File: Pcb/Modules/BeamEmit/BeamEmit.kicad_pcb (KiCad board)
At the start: 2 copper layers, 50.8 x 20.3 mm, 10 parts, among them J1 JACK_RJ45, Q1 Q_NMOS_GSD, U3 TSOP585xx

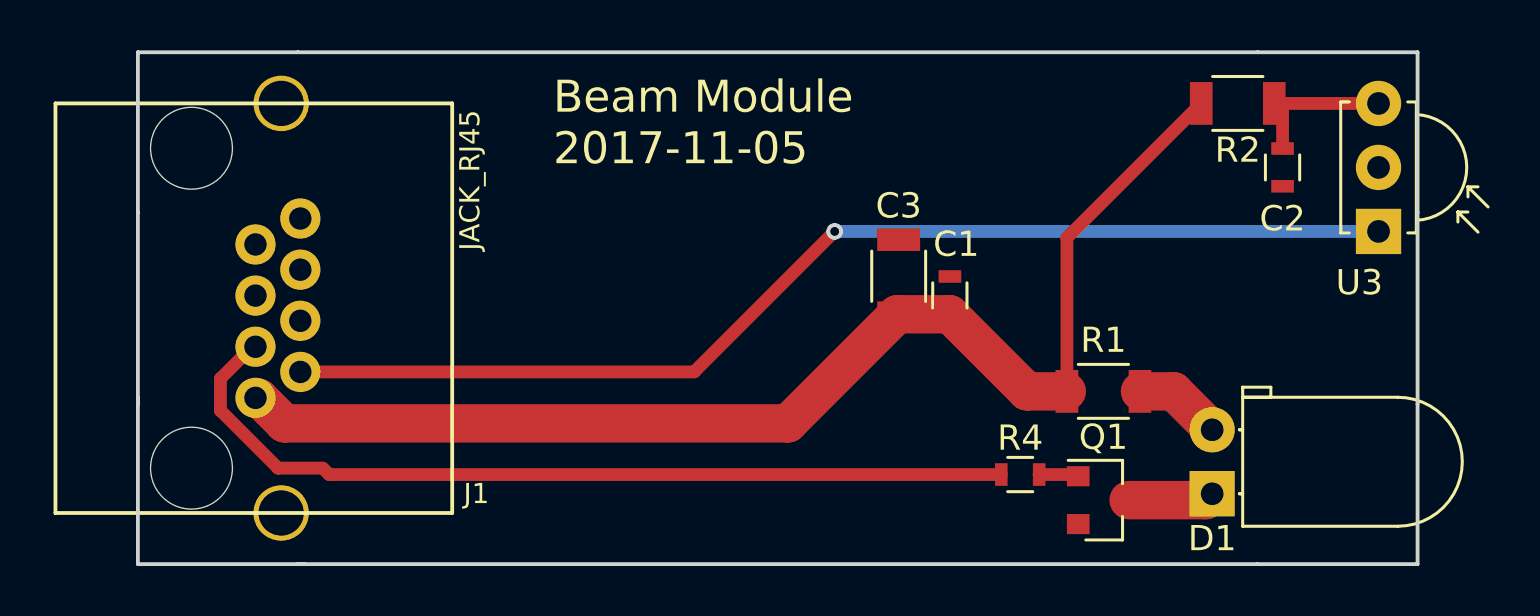
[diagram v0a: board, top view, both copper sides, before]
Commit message: Update module pcbs
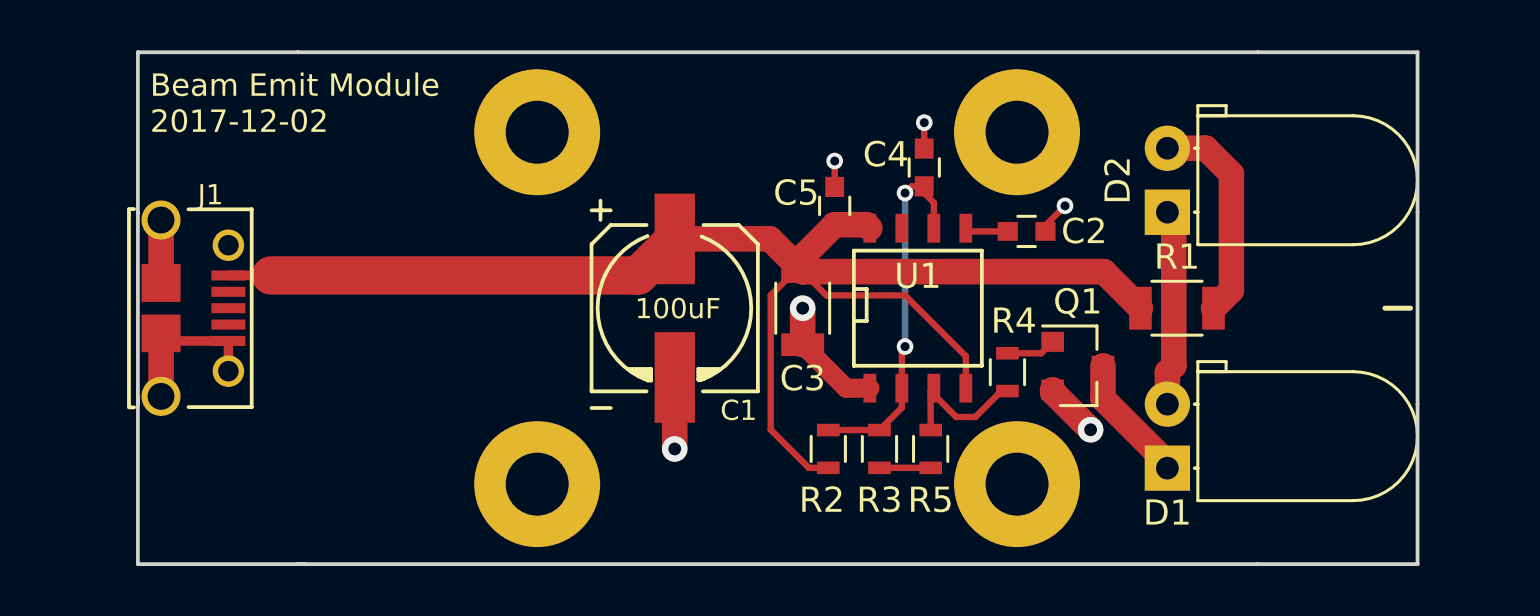
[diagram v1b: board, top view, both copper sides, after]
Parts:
- removed U3: TSOP585xx, Opto-Devices:IRReceiver_Vishay_MINICAST-3pin
- added C4: 1nF, Capacitors_SMD:C_0603, F.Cu at (66.8, 40.1)
- added C5: 0.1uF, Capacitors_SMD:C_0603, F.Cu at (63.2, 41.7)
- added D2: IR_LED, LEDs:LED_D5.0mm_Horizontal_O1.27mm_Z15.0mm, F.Cu at (76.5, 41.9)
- added R3: 10K, Resistors_SMD:R_0603, F.Cu at (65.0, 51.3)
- added R5: 10K, Resistors_SMD:R_0603, F.Cu at (67.1, 51.3)
- added U1: LM555N, SMD_Packages:SOIC-8-N, F.Cu at (66.5, 45.7)
- added X1: HOLE, Mounting_Holes:MountingHole_2.5mm_Pad, F.Cu at (51.4, 38.7)
- added X2: HOLE, Mounting_Holes:MountingHole_2.5mm_Pad, F.Cu at (51.4, 52.7)
- added X3: HOLE, Mounting_Holes:MountingHole_2.5mm_Pad, F.Cu at (70.5, 38.7)
- added X4: HOLE, Mounting_Holes:MountingHole_2.5mm_Pad, F.Cu at (70.5, 52.7)
- C1: value 0.1uF -> 100uF; footprint Resistors_SMD:R_0603 -> CA6:c_elec_6.3x5.7
- C2: footprint Resistors_SMD:R_0603 -> Capacitors_SMD:C_0603
- C3: value 10uF -> e10uF
- J1: value JACK_RJ45 -> MICRO_USB; footprint CA6:RJ45_pcbwing -> CA6:USB_MICRO_10118194-0001LF
- R1: value 20R -> 22R
- R2: value 20R -> 100K; footprint Resistors_SMD:R_1206 -> Resistors_SMD:R_0603
- moved R2 21.3 mm to (63.0, 51.3), turned to 270 degrees
- moved C1 10.9 mm to (56.9, 45.7)
- moved C2 10.5 mm to (70.9, 42.7), turned to 0 degrees
- moved Q1 5.43 mm to (72.9, 48.0)
- moved J1 5.08 mm to (35.1, 45.7)
- moved R1 4.41 mm to (76.8, 45.7)
- moved R4 4.10 mm to (70.1, 48.3), turned to 90 degrees
- moved C3 4.02 mm to (62.0, 45.7), turned to 270 degrees
- moved D1 2.05 mm to (76.5, 52.1)
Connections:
- net +3V3 renamed +5V
- J1 pad 2: Net-(J1-Pad2) -> (no net)
- J1 pad 3: Net-(J1-Pad3) -> (no net)
- J1 pad 5: (no net) -> GND
- R1 pad 1: Net-(D1-Pad2) -> Net-(D2-Pad2)
- R2 pad 1: Net-(C2-Pad1) -> Net-(C4-Pad1)
- R4 pad 1: Net-(J1-Pad3) -> Net-(R4-Pad1)
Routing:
- net Net-(J1-Pad2): track 45.1 -> 0.00 mm, vias 1 -> 0
- net Net-(J1-Pad3): track 35.2 -> 0.00 mm
- net GND: track 0.00 -> 22.3 mm, vias 0 -> 6
- net Net-(C4-Pad1): track 0.00 -> 14.6 mm, vias 0 -> 2
- net +5V: track 49.3 -> 60.9 mm
- net Net-(D2-Pad2): track 0.00 -> 8.59 mm
- net Net-(R4-Pad1): track 0.00 -> 5.68 mm
- net Net-(C2-Pad1): track 6.06 -> 1.72 mm
- net Net-(D1-Pad2): track 3.50 -> 7.83 mm
- net Net-(R3-Pad2): track 0.00 -> 2.03 mm
- net Net-(D1-Pad1): track 3.42 -> 5.12 mm
- removed copper zone on F.Cu, net GND
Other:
- net class Default: clearance 0.254 -> 0.2032
- rule trace_clearance: 0.254 -> 0.2032
- board text added: "Beam Emit Module 2017-12-02"
- board text removed: "Beam Module 2017-11-05"

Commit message: Update pcbs.
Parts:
- C3: value e10uF -> 10uF
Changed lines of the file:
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@@
   )
   (setup
-    (last_trace_width 1.524)
+    (last_trace_width 0.254)
     (user_trace_width 0.381)
     (user_trace_width 0.508)
@@
       (effects (font (size 1 1) (thickness 0.15)))
     )
-    (fp_text value e10uF (at -0.254 -1.778 270) (layer F.Fab) hide
+    (fp_text value 10uF (at -0.254 -1.778 270) (layer F.Fab) hide
       (effects (font (size 1 1) (thickness 0.15)))
     )

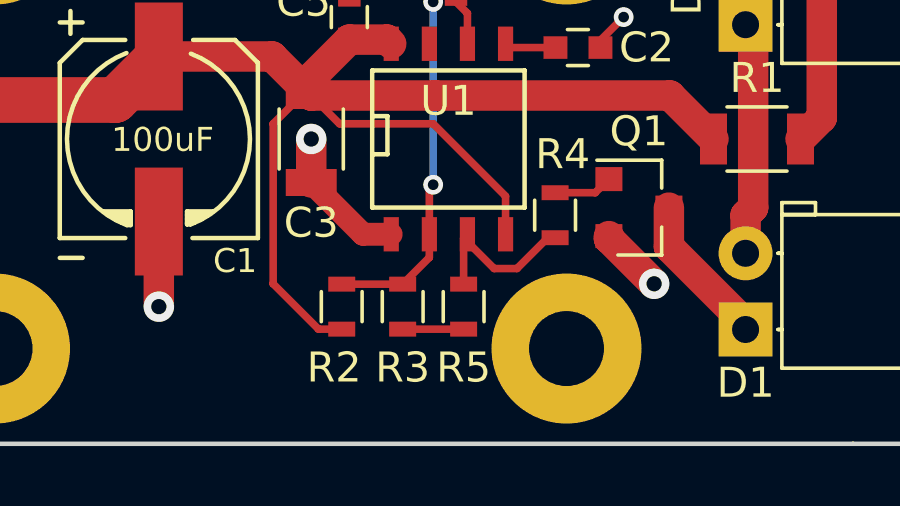
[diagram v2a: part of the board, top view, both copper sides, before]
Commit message: Update beam emitter to use single 20k
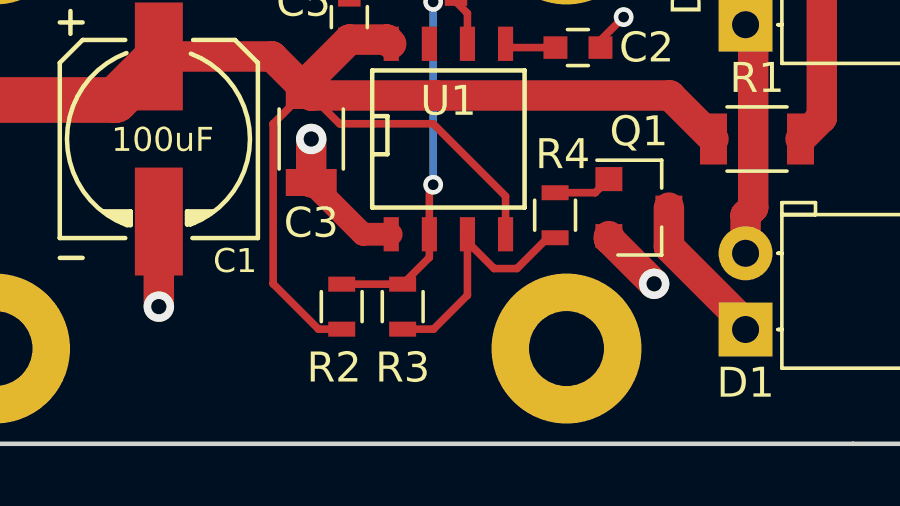
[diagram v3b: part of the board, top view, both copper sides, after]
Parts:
- removed R5: 10K, Resistors_SMD:R_0603
- R3: value 10K -> 20K
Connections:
- R4 pad 1: Net-(R4-Pad1) -> Net-(R3-Pad2)
- U1 pad 3: Net-(R4-Pad1) -> Net-(R3-Pad2)
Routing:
- net Net-(R3-Pad2): track 2.03 -> 8.81 mm
- net Net-(R4-Pad1): track 5.68 -> 0.00 mm
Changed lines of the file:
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@@
 (kicad_pcb (version 4) (host pcbnew 4.0.5)
   (general
-    (links 32)
+    (links 31)
     (no_connects 0)
     (area 35.510399 35.484999 86.460401 55.955001)
     (thickness 1.6)
     (drawings 14)
-    (tracks 79)
+    (tracks 80)
     (zones 0)
-    (modules 19)
-    (nets 11)
+    (modules 18)
+    (nets 10)
   )
   (page A4)
@@
   (net 8 "Net-(D2-Pad2)")
   (net 9 "Net-(R3-Pad2)")
-  (net 10 "Net-(R4-Pad1)")
   (net_class Default "This is the default net class."
     (clearance 0.2032)
@@
     (add_net "Net-(Q1-Pad1)")
     (add_net "Net-(R3-Pad2)")
-    (add_net "Net-(R4-Pad1)")
   )
   (module TO_SOT_Packages_SMD:SOT-23 (layer F.Cu)
@@
     (fp_line (start 1.25 0.7) (end -1.25 0.7) (layer F.CrtYd) (width 0.05))
     (pad 1 smd rect (at -0.75 0 90) (size 0.5 0.9) (layers F.Cu F.Paste F.Mask)
-      (net 10 "Net-(R4-Pad1)"))
+      (net 9 "Net-(R3-Pad2)"))
     (pad 2 smd rect (at 0.75 0 90) (size 0.5 0.9) (layers F.Cu F.Paste F.Mask)
       (net 1 "Net-(Q1-Pad1)"))
@@
       (effects (font (size 1 1) (thickness 0.15)))
     )
-    (fp_text value 10K (at 0 1.5 270) (layer F.Fab) hide
+    (fp_text value 20K (at 0 1.5 270) (layer F.Fab) hide
       (effects (font (size 1 1) (thickness 0.15)))
     )
@@
     (pad 2 smd rect (at 0.75 0 270) (size 0.5 0.9) (layers F.Cu F.Paste F.Mask)
       (net 9 "Net-(R3-Pad2)"))
-    (model ${KISYS3DMOD}/Resistors_SMD.3dshapes/R_0603.wrl
-      (at (xyz 0 0 0))
-      (scale (xyz 1 1 1))
-      (rotate (xyz 0 0 0))
-    )
-  )
-  (module Resistors_SMD:R_0603 (layer F.Cu)
-    (at 67.056 51.308 90)
-    (descr "Resistor SMD 0603, reflow soldering, Vishay (see dcrcw.pdf)")
-    (tags "resistor 0603")
-    (attr smd)
-    (fp_text reference R5 (at -2.032 0 180) (layer F.SilkS)
-      (effects (font (size 1 1) (thickness 0.15)))
-    )
-    (fp_text value 10K (at 0 1.5 90) (layer F.Fab) hide
-      (effects (font (size 1 1) (thickness 0.15)))
-    )
-    (fp_text user %R (at 0 0 90) (layer F.Fab)
-      (effects (font (size 0.4 0.4) (thickness 0.075)))
-    )
-    (fp_line (start -0.8 0.4) (end -0.8 -0.4) (layer F.Fab) (width 0.1))
-    (fp_line (start 0.8 0.4) (end -0.8 0.4) (layer F.Fab) (width 0.1))
-    (fp_line (start 0.8 -0.4) (end 0.8 0.4) (layer F.Fab) (width 0.1))
-    (fp_line (start -0.8 -0.4) (end 0.8 -0.4) (layer F.Fab) (width 0.1))
-    (fp_line (start 0.5 0.68) (end -0.5 0.68) (layer F.SilkS) (width 0.12))
-    (fp_line (start -0.5 -0.68) (end 0.5 -0.68) (layer F.SilkS) (width 0.12))
-    (fp_line (start -1.25 -0.7) (end 1.25 -0.7) (layer F.CrtYd) (width 0.05))
-    (fp_line (start -1.25 -0.7) (end -1.25 0.7) (layer F.CrtYd) (width 0.05))
-    (fp_line (start 1.25 0.7) (end 1.25 -0.7) (layer F.CrtYd) (width 0.05))
-    (fp_line (start 1.25 0.7) (end -1.25 0.7) (layer F.CrtYd) (width 0.05))
-    (pad 1 smd rect (at -0.75 0 90) (size 0.5 0.9) (layers F.Cu F.Paste F.Mask)
-      (net 9 "Net-(R3-Pad2)"))
-    (pad 2 smd rect (at 0.75 0 90) (size 0.5 0.9) (layers F.Cu F.Paste F.Mask)
-      (net 10 "Net-(R4-Pad1)"))
     (model ${KISYS3DMOD}/Resistors_SMD.3dshapes/R_0603.wrl
       (at (xyz 0 0 0))
@@
       (net 6 +5V))
     (pad 3 smd rect (at 0.635 3.175) (size 0.508 1.143) (layers F.Cu F.Paste F.Mask)
-      (net 10 "Net-(R4-Pad1)"))
+      (net 9 "Net-(R3-Pad2)"))
     (pad 2 smd rect (at -0.635 3.175) (size 0.508 1.143) (layers F.Cu F.Paste F.Mask)
       (net 7 "Net-(C4-Pad1)"))
@@
   (segment (start 78.994 40.386) (end 78.994 45.011) (width 1.016) (layer F.Cu) (net 8))
   (segment (start 77.978 39.37) (end 78.994 40.386) (width 1.016) (layer F.Cu) (net 8))
-  (segment (start 67.056 52.058) (end 65.024 52.058) (width 0.254) (layer F.Cu) (net 9))
-  (segment (start 70.104 49.01) (end 69.862 49.01) (width 0.254) (layer F.Cu) (net 10))
-  (segment (start 69.862 49.01) (end 68.834 50.038) (width 0.254) (layer F.Cu) (net 10))
-  (segment (start 68.834 50.038) (end 68.072 50.038) (width 0.254) (layer F.Cu) (net 10))
-  (segment (start 68.072 50.038) (end 67.183 49.149) (width 0.254) (layer F.Cu) (net 10))
-  (segment (start 67.183 49.149) (end 67.183 48.895) (width 0.254) (layer F.Cu) (net 10))
-  (segment (start 67.056 50.558) (end 67.056 49.022) (width 0.254) (layer F.Cu) (net 10))
-  (segment (start 67.056 49.022) (end 67.183 48.895) (width 0.254) (layer F.Cu) (net 10))
+  (segment (start 67.183 48.895) (end 67.183 50.927) (width 0.254) (layer F.Cu) (net 9))
+  (segment (start 66.052 52.058) (end 65.024 52.058) (width 0.254) (layer F.Cu) (net 9))
+  (segment (start 67.183 50.927) (end 66.052 52.058) (width 0.254) (layer F.Cu) (net 9))
+  (segment (start 70.104 49.01) (end 69.862 49.01) (width 0.254) (layer F.Cu) (net 9))
+  (segment (start 69.862 49.01) (end 68.834 50.038) (width 0.254) (layer F.Cu) (net 9))
+  (segment (start 68.834 50.038) (end 68.072 50.038) (width 0.254) (layer F.Cu) (net 9))
+  (segment (start 68.072 50.038) (end 67.183 49.149) (width 0.254) (layer F.Cu) (net 9))
+  (segment (start 67.183 49.149) (end 67.183 48.895) (width 0.254) (layer F.Cu) (net 9))
+  (segment (start 67.056 49.022) (end 67.183 48.895) (width 0.254) (layer F.Cu) (net 9))
   (zone (net 2) (net_name GND) (layer B.Cu) (hatch edge 0.508)
     (connect_pads (clearance 0.508))

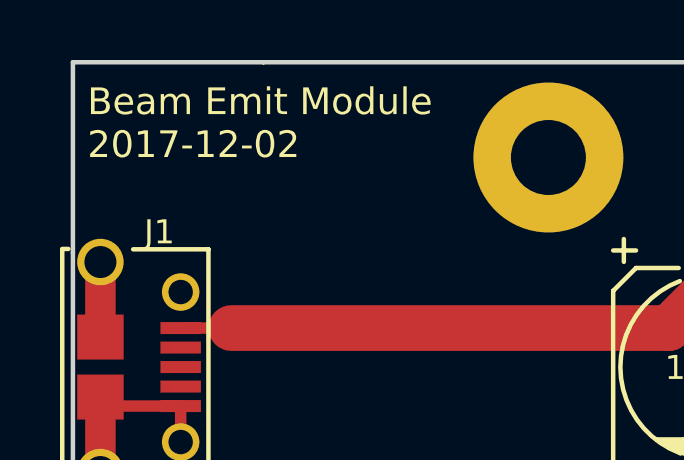
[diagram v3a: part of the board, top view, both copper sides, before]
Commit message: Update CA6 PCB.  Also update versions of all the module pcbs to match.
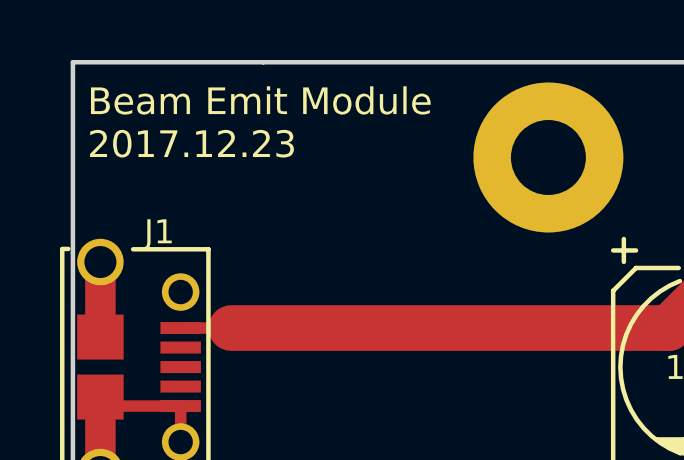
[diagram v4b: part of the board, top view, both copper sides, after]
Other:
- board text added: "Beam Emit Module 2017.12.23"
- board text removed: "Beam Emit Module 2017-12-02"
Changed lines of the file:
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@@
     (links 31)
     (no_connects 0)
-    (area 35.510399 35.484999 86.460401 55.955001)
+    (area 34.5988 34.2568 88.4622 57.2832)
     (thickness 1.6)
     (drawings 14)
@@
   (gr_line (start 35.5854 41.91) (end 35.5854 49.53) (angle 90) (layer Edge.Cuts) (width 0.15))
   (gr_line (start 86.3854 41.91) (end 86.3854 49.53) (angle 90) (layer Edge.Cuts) (width 0.15))
-  (gr_text "Beam Emit Module\n2017-12-02" (at 36.068 37.592) (layer F.SilkS)
+  (gr_text "Beam Emit Module\n2017.12.23" (at 36.068 37.592) (layer F.SilkS)
     (effects (font (size 0.889 0.889) (thickness 0.2032)) (justify left))
   )

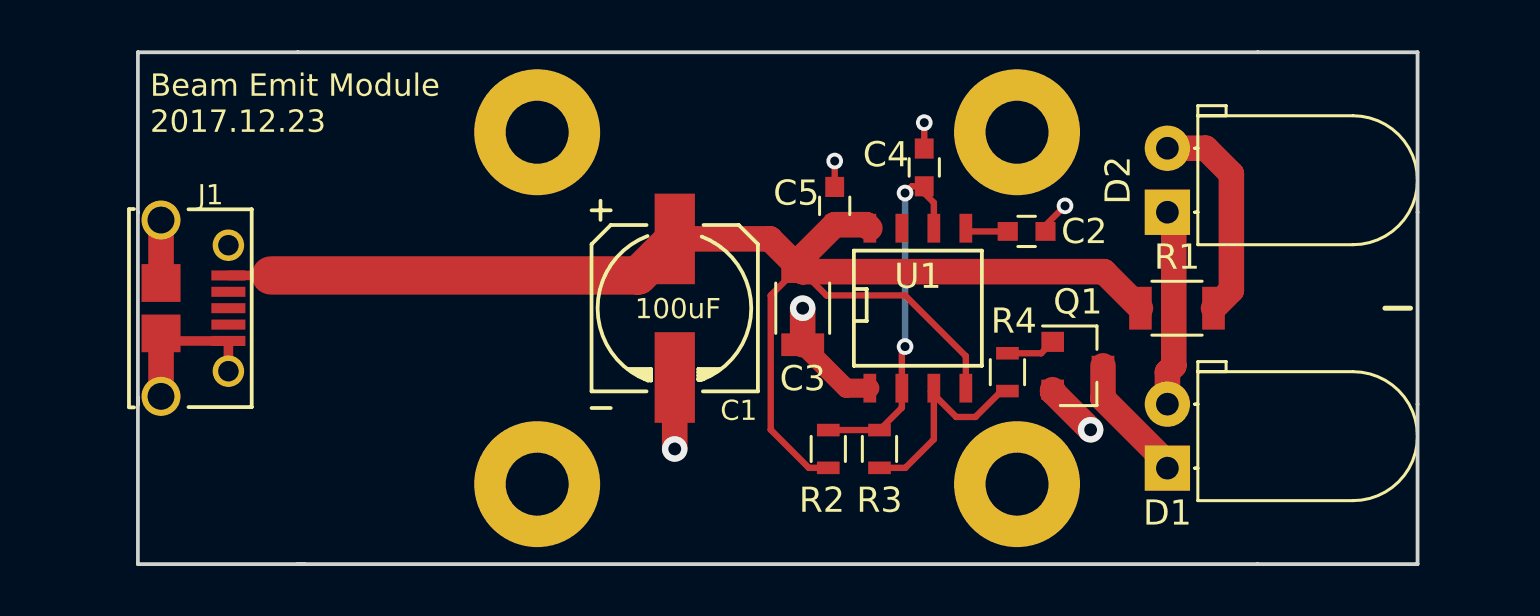
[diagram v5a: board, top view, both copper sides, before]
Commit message: Update module pcbs
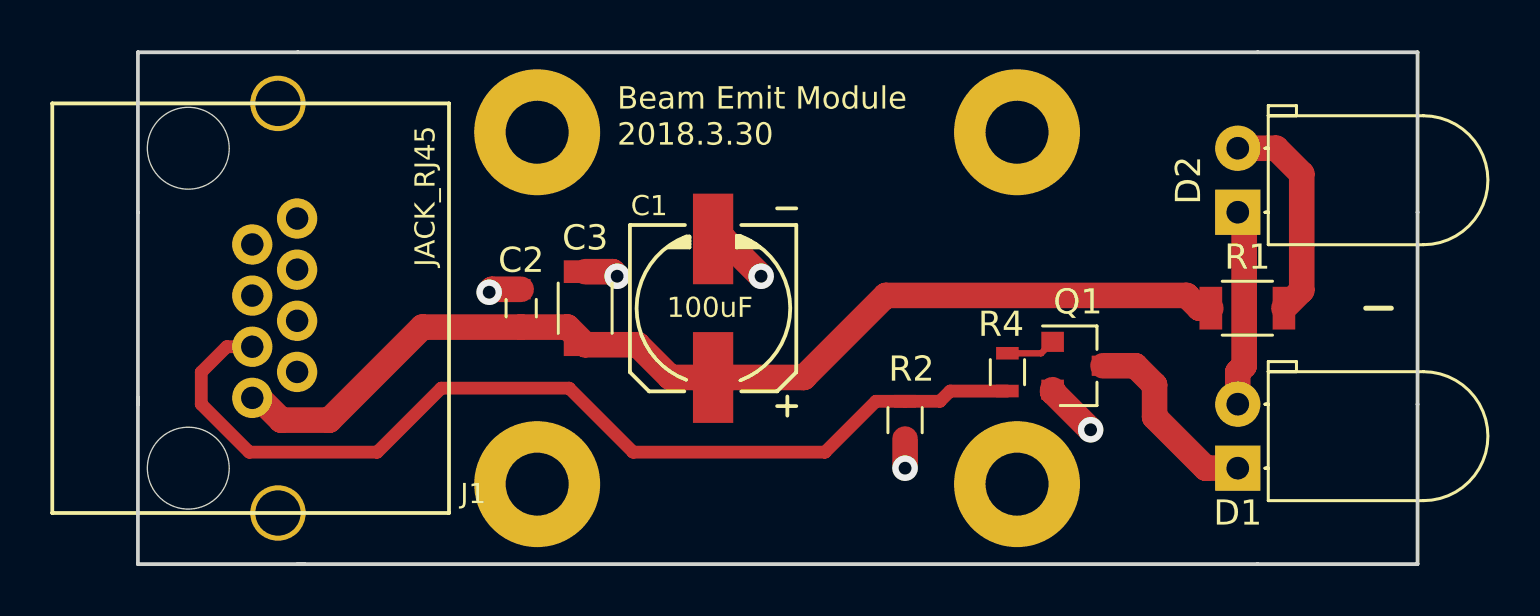
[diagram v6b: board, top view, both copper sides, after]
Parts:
- removed C4: 1nF, Capacitors_SMD:C_0603
- removed C5: 0.1uF, Capacitors_SMD:C_0603
- removed R3: 20K, Resistors_SMD:R_0603
- removed U1: LM555N, SMD_Packages:SOIC-8-N
- J1: value MICRO_USB -> JACK_RJ45; footprint CA6:USB_MICRO_10118194-0001LF -> CA6:RJ45_pcbwing
- R1: value 22R -> 4R7
- moved C2 20.3 mm to (50.8, 45.7), turned to 90 degrees
- moved C3 8.64 mm to (53.3, 45.7), turned to 90 degrees
- moved J1 4.95 mm to (40.0, 45.7)
- moved R2 3.26 mm to (66.0, 50.2), turned to 90 degrees
- moved D1 2.79 mm to (79.2, 52.1)
- moved D2 2.79 mm to (79.2, 41.9)
- moved R1 2.79 mm to (79.6, 45.7)
- moved C1 1.52 mm to (58.4, 45.7), turned to 270 degrees
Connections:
- C1 pad 1: +5V -> +3V3
- C2 pad 1: Net-(C2-Pad1) -> +3V3
- C3 pad 1: +5V -> +3V3
- J1 pad 1: +5V -> +3V3
- J1 pad 3: (no net) -> Net-(J1-Pad3)
- J1 pad 5: GND -> (no net)
- R1 pad 2: +5V -> +3V3
- R2 pad 1: Net-(C4-Pad1) -> GND
- R2 pad 2: +5V -> Net-(J1-Pad3)
- R4 pad 1: Net-(R3-Pad2) -> Net-(J1-Pad3)
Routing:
- net +5V: track 60.9 -> 0.00 mm
- net +3V3: track 0.00 -> 42.8 mm
- net Net-(J1-Pad3): track 0.00 -> 39.9 mm
- net Net-(C4-Pad1): track 14.6 -> 0.00 mm, vias 2 -> 0
- net GND: track 22.3 -> 8.55 mm, vias 6 -> 5
- net Net-(R3-Pad2): track 8.81 -> 0.00 mm
- net Net-(D1-Pad1): track 5.12 -> 7.98 mm
- net Net-(C2-Pad1): track 1.72 -> 0.00 mm
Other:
- board text added: "Beam Emit Module 2018.3.30"
- board text removed: "Beam Emit Module 2017.12.23"

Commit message: Move holes on sound module to match other modules.  Updated silkscreens on other modules.  Generate gerbers
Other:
- board text added: "Beam Emit Module 2018.3.31"
- board text removed: "Beam Emit Module 2018.3.30"
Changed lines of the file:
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@@
     (links 17)
     (no_connects 0)
-    (area 31.906869 34.2568 88.4622 57.2832)
+    (area 31.906869 34.2568 91.2562 57.2832)
     (thickness 1.6)
     (drawings 14)
@@
   )
   (setup
-    (last_trace_width 1.016)
+    (last_trace_width 0.254)
     (user_trace_width 0.381)
     (user_trace_width 0.508)
@@
   (gr_line (start 35.5854 41.91) (end 35.5854 49.53) (angle 90) (layer Edge.Cuts) (width 0.15))
   (gr_line (start 86.3854 41.91) (end 86.3854 49.53) (angle 90) (layer Edge.Cuts) (width 0.15))
-  (gr_text "Beam Emit Module\n2018.3.30" (at 54.61 38.1) (layer F.SilkS)
+  (gr_text "Beam Emit Module\n2018.3.31" (at 54.61 38.1) (layer F.SilkS)
     (effects (font (size 0.889 0.889) (thickness 0.2032)) (justify left))
   )
